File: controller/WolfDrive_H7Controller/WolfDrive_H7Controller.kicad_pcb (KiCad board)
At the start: 4 copper layers, 167.6 x 111.8 mm, 281 parts, among them CN10 CONN_02X17, CN7 CONN_02X10, CN8 CONN_02X08, CN9 CONN_02X15, CON1 SD_Card, J1 USB_OTG, J10 GND, J11 GND, J12 5V, J13 Regen, J14 Throttle, J15 PWM1, J16 PWM2, J17 PWM3, J18 ~PWM1, J19 ~PWM2, J2 QSPI_CLK, J20 ~PWM3, J21 OCV, J22 ~F_C, J23 ~F_B, J24 ~F_A, J25 Overtemp, J26 PWM1, J27 Conn_01x04_Female, J29 Conn_01x04, J3 QSPI_NCS, J30 SPI2_SCK, J31 SPI2_NSS, J32 SPI2_MOSI, J33 SPI2_MISO, J34 PS-DIS, J35 3V3, J36 GND, J37 GND, J38 AGND, J39 SP1_MISO, J4 QSPI_IO0, J40 SP1_SCK, J41 SP1_NSS, J42 SP1_MOSI, J43 DB15_Female_HighDensity_Mount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, J5 QSPI_IO1, J6 QSPI_IO2, J7 QSPI_IO3, J8 12V, J9 GND, P10 GATE_IO_A, P11 GATE_IO_A, P7 CONN_01X02, P9 GATE_IO_A, Q2 Q_NMOS_DGS, U1 LM1117-5.0, U10 74LS136, U11 FT232RL, U2 LM1117-3.3, U3 MCP101-315D, U4 LTV-356T, U5 ISO7221, U7 OPA2340, U8 LM339, U9 CD4044B

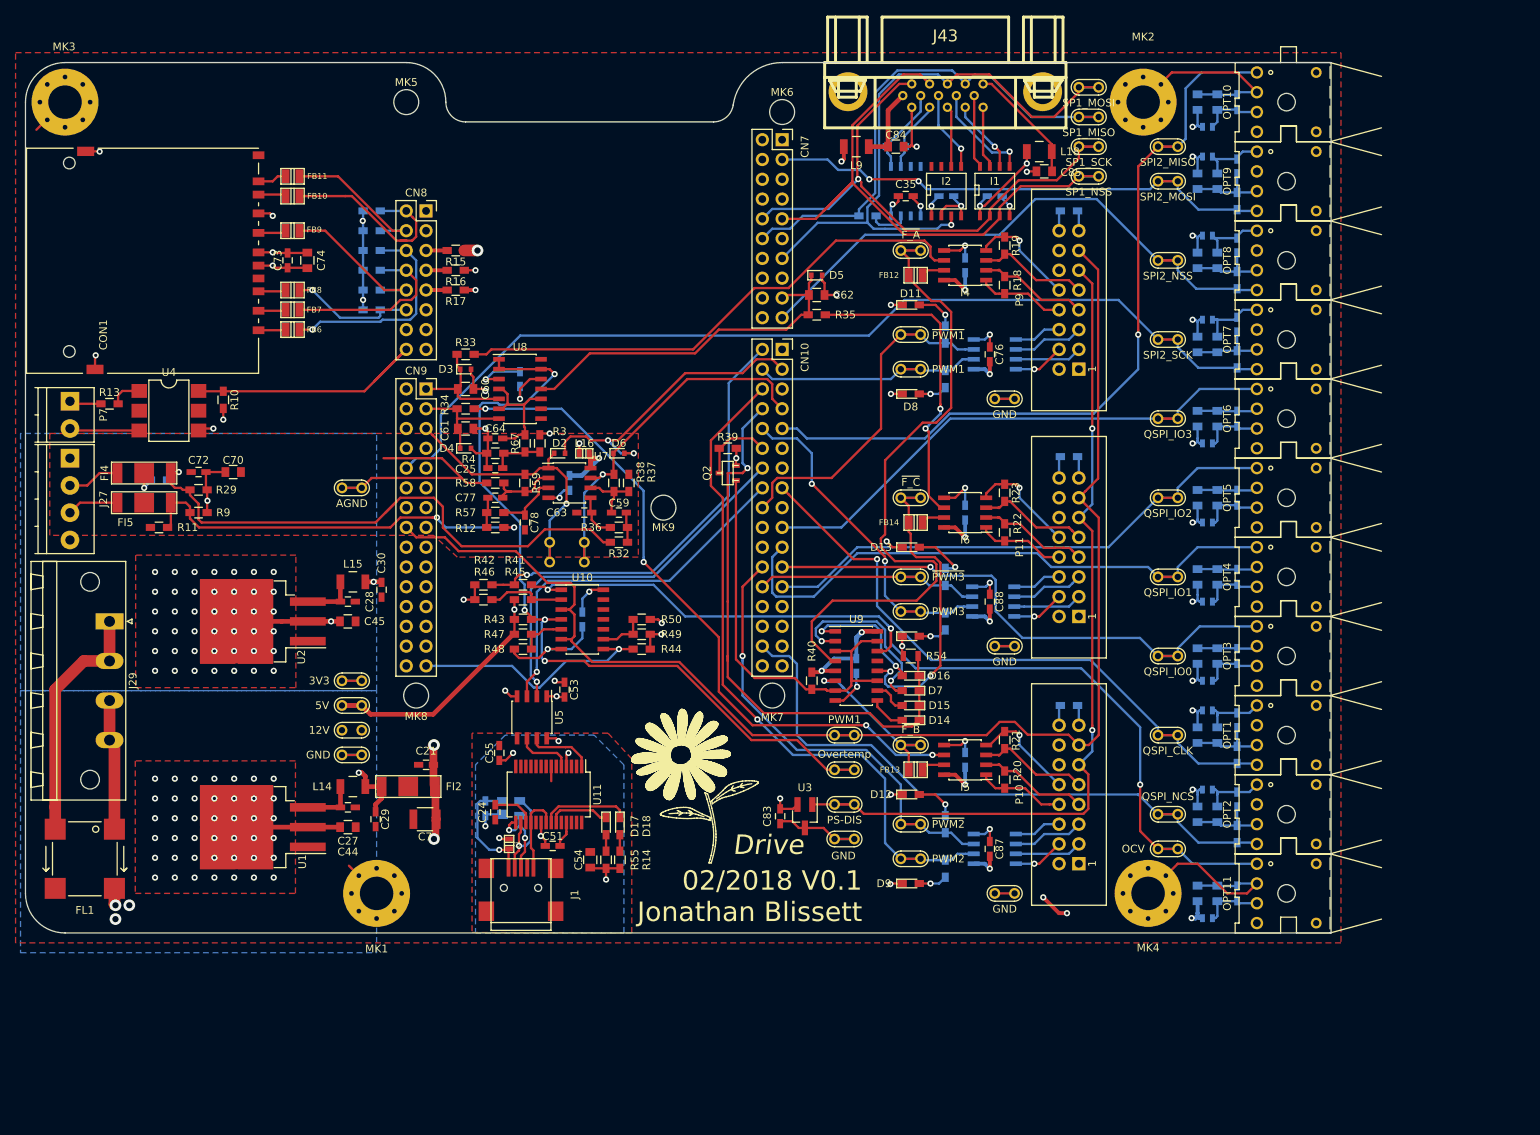
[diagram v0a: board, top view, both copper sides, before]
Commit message: PCB layout progress for issues <5
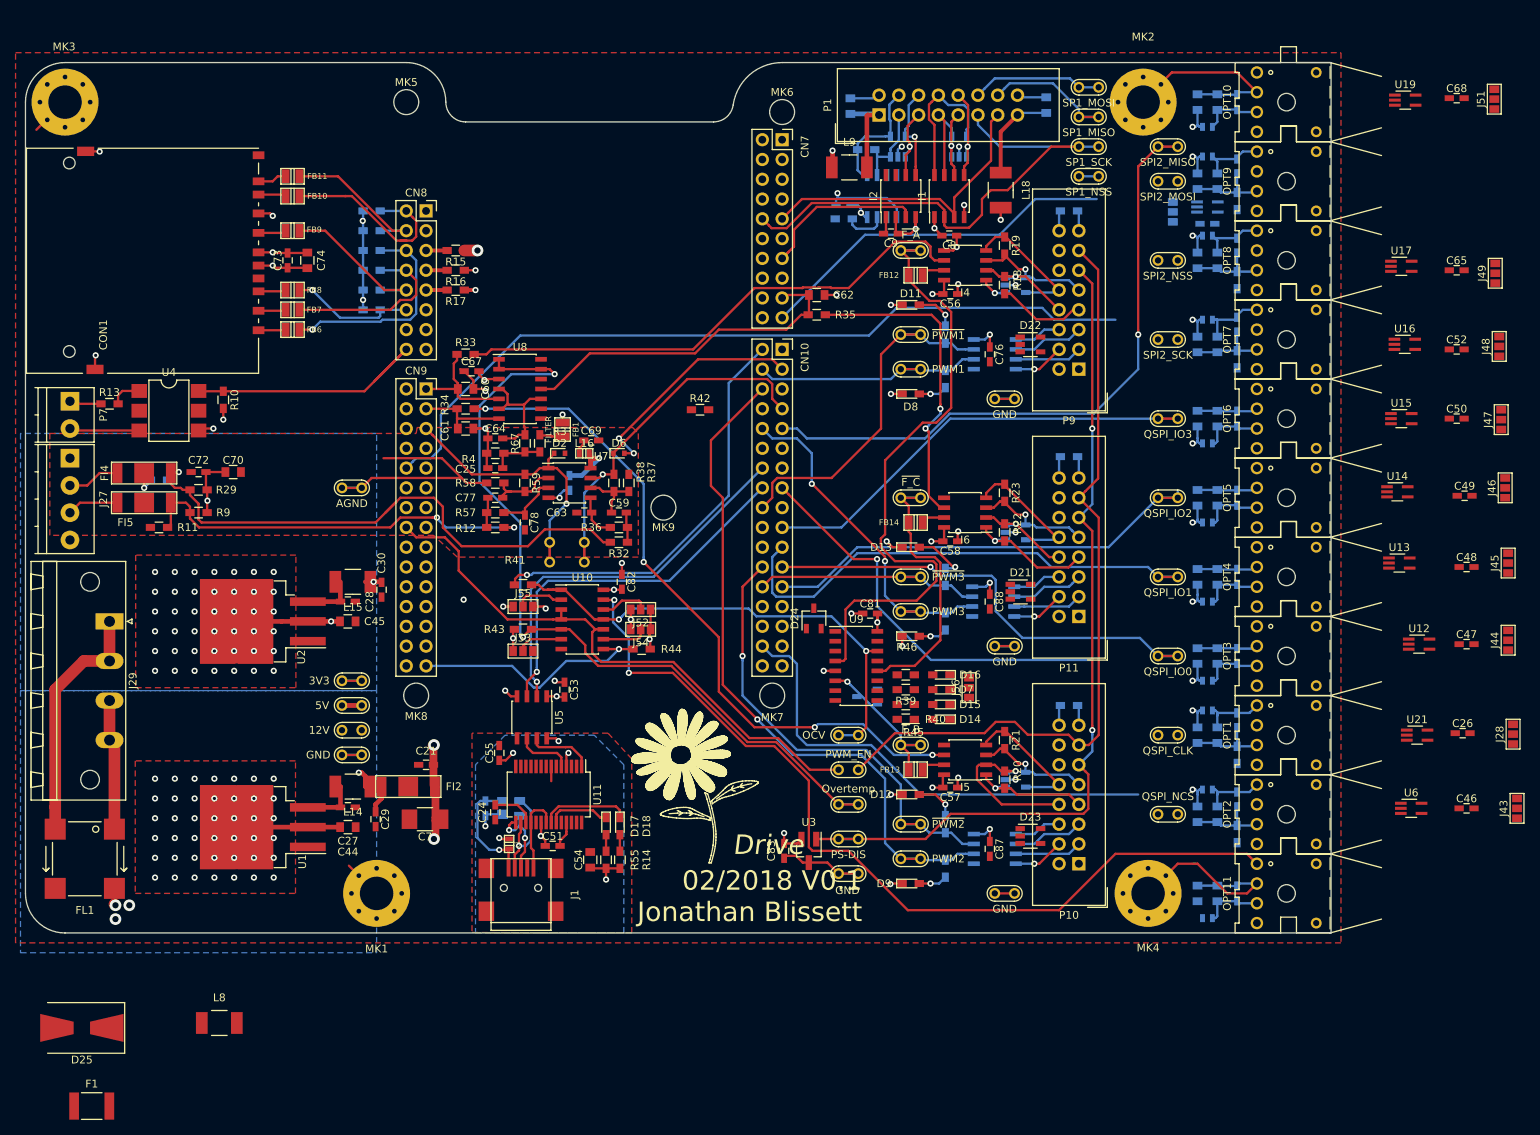
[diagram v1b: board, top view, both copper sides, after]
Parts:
- removed Q2: Q_NMOS_DGS, w_smd_trans:sot23
- removed R47, R48, R49, R50: 10k, Resistors_SMD:R_0603_HandSoldering
- removed R54: 47, Resistors_SMD:R_0805
- added C26: 10n, Capacitors_SMD:C_0603_HandSoldering, F.Cu at (134.4, 4.83)
- added C46: 10n, Capacitors_SMD:C_0603_HandSoldering, F.Cu at (134.9, 14.5)
- added C47: 10n, Capacitors_SMD:C_0603_HandSoldering, F.Cu at (134.9, -6.60)
- added C48: 10n, Capacitors_SMD:C_0603_HandSoldering, F.Cu at (134.9, -16.5)
- added C49: 10n, Capacitors_SMD:C_0603_HandSoldering, F.Cu at (134.6, -25.7)
- added C50: 10n, Capacitors_SMD:C_0603_HandSoldering, F.Cu at (133.6, -35.6)
- added C52: 10n, Capacitors_SMD:C_0603_HandSoldering, F.Cu at (133.6, -44.5)
- added C65: 10n, Capacitors_SMD:C_0603_HandSoldering, F.Cu at (133.6, -54.6)
- added C66: 10n, Capacitors_SMD:C_0603_HandSoldering, B.Cu at (101.6, -60.6)
- added C68: 10n, Capacitors_SMD:C_0603_HandSoldering, F.Cu at (133.6, -76.7)
- added C69: 1u, Capacitors_SMD:C_0603_HandSoldering, F.Cu at (22.5, -32.8)
- added D19: SP0504BAHT, TO_SOT_Packages_SMD:TSOT-23-5, B.Cu at (77.0, 10.8)
- added D20: SP0504BAHT, TO_SOT_Packages_SMD:TSOT-23-5, B.Cu at (77.0, -21.0)
- added D21: SP0504BAHT, TO_SOT_Packages_SMD:TSOT-23-5, F.Cu at (77.6, -13.3)
- added D22: SP0504BAHT, TO_SOT_Packages_SMD:TSOT-23-5, F.Cu at (78.9, -45.1)
- added D23: SP0504BAHT, TO_SOT_Packages_SMD:TSOT-23-5, F.Cu at (78.9, 18.0)
- added D24: D_Schottky_x2_KCom_AAK, TO_SOT_Packages_SMD:TSOT-23, F.Cu at (51.1, -9.91)
- added D25: 1.5KExxA, Diode_SMD:D_SMB-SMC_Universal_Handsoldering, F.Cu at (-42.9, 42.7)
- added D26: D_Schottky_x2_KCom_AAK, TO_SOT_Packages_SMD:TSOT-23, B.Cu at (57.9, 0.13)
- added F1: Polyfuse, Fuse:Fuse_1812_4532Metric_Pad1.24x3.50mm_HandSolder, F.Cu at (-41.7, 52.7)
- added FB1: FILTER, w_smd_inductors:inductor_smd_0805, F.Cu at (18.8, -34.2)
- added J28: GS3, Connectors:GS3, F.Cu at (140.8, 4.95)
- added J44: GS3, Connectors:GS3, F.Cu at (140.2, -7.11)
- added J45: GS3, Connectors:GS3, F.Cu at (140.2, -17.0)
- added J46: GS3, Connectors:GS3, F.Cu at (139.8, -26.7)
- added J47: GS3, Connectors:GS3, F.Cu at (139.3, -35.4)
- added J48: GS3, Connectors:GS3, F.Cu at (139.1, -44.8)
- added J49: GS3, Connectors:GS3, F.Cu at (138.6, -54.2)
- added J50: GS3, Connectors:GS3, B.Cu at (97.2, -62.1)
- added J51: GS3, Connectors:GS3, F.Cu at (138.4, -76.6)
- added J52: GS3, Connectors:GS3, F.Cu at (28.8, -11.0)
- added J53: GS3, Connectors:GS3, F.Cu at (13.7, -5.71)
- added J54: GS3, Connectors:GS3, F.Cu at (28.8, -8.51)
- added J55: GS3, Connectors:GS3, F.Cu at (13.7, -11.4)
- added J56: GS3, Connectors:GS3, F.Cu at (71.0, -1.02)
- added L8: 10uH, Inductors_NEOSID:Neosid_Inductor_SM-NE45_SMD1812, F.Cu at (-25.3, 42.0)
- added P1: GATE_IO_A, Connectors_IDC:IDC-Header_2x08_Pitch2.54mm_Straight, F.Cu at (59.4, -74.5)
- added U12: 74LVC1G02, TO_SOT_Packages_SMD:SOT-353_SC-70-5_Handsoldering, F.Cu at (128.8, -6.60)
- added U13: 74LVC1G02, TO_SOT_Packages_SMD:SOT-353_SC-70-5_Handsoldering, F.Cu at (126.2, -17.0)
- added U14: 74LVC1G02, TO_SOT_Packages_SMD:SOT-353_SC-70-5_Handsoldering, F.Cu at (126.0, -26.2)
- added U15: 74LVC1G02, TO_SOT_Packages_SMD:SOT-353_SC-70-5_Handsoldering, F.Cu at (126.5, -35.6)
- added U16: 74LVC1G02, TO_SOT_Packages_SMD:SOT-353_SC-70-5_Handsoldering, F.Cu at (126.9, -45.1)
- added U17: 74LVC1G02, TO_SOT_Packages_SMD:SOT-353_SC-70-5_Handsoldering, F.Cu at (126.5, -55.1)
- added U18: 74LVC1G02, TO_SOT_Packages_SMD:SOT-353_SC-70-5_Handsoldering, B.Cu at (101.6, -62.7)
- added U19: 74LVC1G02, TO_SOT_Packages_SMD:SOT-353_SC-70-5_Handsoldering, F.Cu at (127.0, -76.5)
- added U21: 74LVC1G02, TO_SOT_Packages_SMD:SOT-353_SC-70-5_Handsoldering, F.Cu at (128.5, 5.08)
- added U6: 74LVC1G02, TO_SOT_Packages_SMD:SOT-353_SC-70-5_Handsoldering, F.Cu at (127.8, 14.5)
- C27, C28: value 100n -> 1u
- C29: value 1u -> 100n
- C35, C84, C85: moved to B.Cu
- C56, C57, C58, C67, C8, C81, C82, C9: moved to F.Cu
- C7: footprint Capacitors_SMD:C_1210 -> Capacitors_SMD:C_1210_HandSoldering
- D3, D4, D5: value 3.3V -> SP0504BAHT; footprint Diodes_SMD:D_SOD-523 -> TO_SOT_Packages_SMD:TSOT-23-5; moved to B.Cu
- I1, I2, I3: footprint SMD_Packages:SOIC-8-N -> Housings_SOIC:SOIC-8_3.9x4.9mm_Pitch1.27mm
- J26: value PWM1 -> PWM_EN
- J43: value DB15_Female_HighDensity_MountingHoles -> GS3; footprint DriveParts:DB_15F-VGA-mountingholes -> Connectors:GS3
- L14, L15, L18, L9: footprint Inductors_NEOSID:Neosid_Inductor_SM-NE30_SMD1210 -> Inductors_NEOSID:Neosid_Inductor_SM-NE45_SMD1812
- P10, P11, P9: footprint Connectors:IDC_Header_Straight_16pins -> Connectors_IDC:IDC-Header_2x08_Pitch2.54mm_Straight
- R33, R34, R35: value 10k -> 4k7
- R39, R40, R45, R46: value 10k -> 680
- R60, R61, R62, R63, R64, R65: value 100 -> 680; footprint LEDs:LED_0603_HandSoldering -> Resistors_SMD:R_0603_HandSoldering
- R8: value 250 -> 240
- U10: value 74LS136 -> 74HC266
- U9: value CD4044B -> CD4043B
- moved J43 119.7 mm to (141.4, 14.5), turned to 0 degrees
- moved D3 69.5 mm to (69.7, -70.5), turned to 90 degrees
- moved D4 67.7 mm to (61.8, -70.5), turned to 90 degrees
- moved R46 55.1 mm to (62.9, -2.67)
- moved R45 51.0 mm to (62.9, 1.14), turned to 180 degrees
- moved J21 43.5 mm to (54.2, 5.08)
- moved R39 38.5 mm to (62.9, -0.76), turned to 180 degrees
- moved R42 35.8 mm to (36.4, -36.7), turned to 0 degrees
- moved D5 25.6 mm to (77.0, -52.7)
- moved R40 13.0 mm to (62.9, 3.05), turned to 180 degrees
- moved C9 8.59 mm to (61.0, -59.3)
- moved C85 8.51 mm to (80.9, -75.8), turned to 90 degrees
- moved C35 8.08 mm to (54.9, -63.0), turned to 0 degrees
- moved C84 7.83 mm to (55.8, -75.7), turned to 90 degrees
- moved C8 7.74 mm to (68.5, -59.1)
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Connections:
- net /5V_thr renamed /12V_thr
- net /~Fault_Gate_A renamed /Fault_Gate_A
- net /~Fault_Gate_B renamed /Fault_Gate_B
- net /~Fault_Gate_C renamed /Fault_Gate_C
- C56 pad 2: +5V -> +3V3
- C57 pad 2: +5V -> +3V3
- C58 pad 2: +5V -> +3V3
- C67 pad 2: +5V -> +3V3
- C76 pad 2: +5V -> +3V3
- C79 pad 2: +5V -> +3V3
- C81 pad 2: +5V -> +3V3
- C82 pad 2: +5V -> +3V3
- C87 pad 2: +5V -> +3V3
- C88 pad 2: +5V -> +3V3
- CN10 pad 1: Net-(CN10-Pad1) -> (no net)
- CN10 pad 11: Net-(CN10-Pad11) -> (no net)
- CN10 pad 13: Net-(CN10-Pad13) -> (no net)
- CN10 pad 20: Net-(CN10-Pad20) -> (no net)
- CN10 pad 28: Net-(CN10-Pad28) -> (no net)
- CN10 pad 29: Net-(CN10-Pad29) -> (no net)
- CN10 pad 30: Net-(CN10-Pad30) -> (no net)
- CN10 pad 31: Net-(CN10-Pad31) -> (no net)
- CN10 pad 33: Net-(CN10-Pad33) -> (no net)
- CN10 pad 34: Net-(CN10-Pad34) -> (no net)
- CN7 pad 1: Net-(CN7-Pad1) -> (no net)
- CN7 pad 11: Net-(CN7-Pad11) -> (no net)
- CN7 pad 14: Net-(CN7-Pad14) -> (no net)
- CN7 pad 15: Net-(CN7-Pad15) -> (no net)
- CN7 pad 16: Net-(CN7-Pad16) -> (no net)
- CN7 pad 18: Net-(CN7-Pad18) -> (no net)
- CN7 pad 2: Net-(CN7-Pad2) -> (no net)
- CN7 pad 20: Net-(CN7-Pad20) -> (no net)
- CN7 pad 4: Net-(CN7-Pad4) -> (no net)
- CN7 pad 5: Net-(CN7-Pad5) -> (no net)
- CN7 pad 6: Net-(CN7-Pad6) -> (no net)
- CN7 pad 7: Net-(CN7-Pad7) -> (no net)
- CN8 pad 1: Net-(CN8-Pad1) -> (no net)
- CN8 pad 14: Net-(CN8-Pad14) -> (no net)
- CN8 pad 15: Net-(CN8-Pad15) -> (no net)
- CN8 pad 3: Net-(CN8-Pad3) -> (no net)
- CN9 pad 11: Net-(CN9-Pad11) -> (no net)
- CN9 pad 12: Net-(CN9-Pad12) -> (no net)
- CN9 pad 13: Net-(CN9-Pad13) -> (no net)
- CN9 pad 14: Net-(CN9-Pad14) -> (no net)
- CN9 pad 15: Net-(CN9-Pad15) -> (no net)
- CN9 pad 17: Net-(CN9-Pad17) -> (no net)
- CN9 pad 18: Net-(CN9-Pad18) -> (no net)
- CN9 pad 19: Net-(CN9-Pad19) -> (no net)
- CN9 pad 2: Net-(CN9-Pad2) -> (no net)
- CN9 pad 20: Net-(CN9-Pad20) -> (no net)
- CN9 pad 21: Net-(CN9-Pad21) -> (no net)
- CN9 pad 22: Net-(CN9-Pad22) -> (no net)
- CN9 pad 24: Net-(CN9-Pad24) -> (no net)
- CN9 pad 25: Net-(CN9-Pad25) -> (no net)
- CN9 pad 26: Net-(CN9-Pad26) -> (no net)
- CN9 pad 27: Net-(CN9-Pad27) -> (no net)
- CN9 pad 28: Net-(CN9-Pad28) -> (no net)
- CN9 pad 30: Net-(CN9-Pad30) -> (no net)
- CN9 pad 4: Net-(CN9-Pad4) -> (no net)
- CN9 pad 6: Net-(CN9-Pad6) -> (no net)
- CN9 pad 7: Net-(CN9-Pad7) -> (no net)
- CN9 pad 8: Net-(CN9-Pad8) -> (no net)
- CON1 pad 10: Net-(CON1-Pad10) -> (no net)
- CON1 pad 11: Net-(CON1-Pad11) -> (no net)
- D14 pad 1: /GPIO_EXTI14_PF14 -> Net-(D14-Pad1)
- D15 pad 1: /GPIO_EXTI14_PF14 -> Net-(D14-Pad1)
- D16 pad 1: /GPIO_EXTI14_PF14 -> Net-(D14-Pad1)
- D3 pad 1: /ADC1_INP15_PA3 -> /SPI1_NSS-
- D4 pad 1: /ADC1_INP10_PC0 -> /SP1_MOSI+
- D5 pad 1: /ADC1_INP18_PA4 -> /Fault_A+
- D7 pad 1: /GPIO_EXTI14_PF14 -> Net-(D14-Pad1)
- FL1 pad 2: +12V -> Net-(D25-Pad1)
- I2 pad 7: Net-(I2-Pad7) -> (no net)
- I2 pad 8: Net-(I2-Pad8) -> (no net)
- I3 pad 3: Net-(I3-Pad3) -> (no net)
- I3 pad 4: Net-(I3-Pad4) -> (no net)
- I3 pad 6: Net-(I3-Pad6) -> (no net)
- I4 pad 1: /~Fault_A- -> /Fault_A+
- I4 pad 2: /~Fault_A+ -> /Fault_A-
- I4 pad 8: +5V -> +3V3
- I5 pad 1: /~Fault_B- -> /Fault_B+
- I5 pad 2: /~Fault_B+ -> /Fault_B-
- I5 pad 8: +5V -> +3V3
- I6 pad 1: /~Fault_C- -> /Fault_C+
- I6 pad 2: /~Fault_C+ -> /Fault_C-
- I6 pad 8: +5V -> +3V3
- I7 pad 1: +5V -> +3V3
- I8 pad 1: +5V -> +3V3
- I9 pad 1: +5V -> +3V3
- J1 pad 4: Net-(J1-Pad4) -> (no net)
- J2 pad 1: /QUADSPI_CLK_PB2 -> Net-(J2-Pad1)
- J21 pad 1: /~Fault_OCV -> /Fault_OCV
- J3 pad 1: /QUADSPI_BK1_NCS_PB10 -> Net-(J3-Pad1)
- J30 pad 1: /SPI2_SCK_PD3 -> Net-(J30-Pad1)
- J31 pad 1: /SPI2_NSS_PB4 -> Net-(J31-Pad1)
- J32 pad 1: /SP2_MOSI_PB15 -> Net-(J32-Pad1)
- J43 pad 2: /SP1_MISO+ -> Net-(J43-Pad2)
- J43 pad 3: /SP1_MOSI+ -> +3V3
- L16 pad 2: +5V -> +12VA
- L17 pad 1: +5V -> +3V3
- OPT1 pad 2: Net-(OPT1-Pad2) -> (no net)
- OPT1 pad 4: /QUADSPI_CLK_PB2 -> Net-(J2-Pad1)
- OPT10 pad 1: /SP2_MISO_PC2 -> Net-(OPT10-Pad1)
- OPT10 pad 4: Net-(OPT10-Pad4) -> (no net)
- OPT11 pad 1: /~Fault_OCV -> Net-(OPT11-Pad1)
- OPT11 pad 4: Net-(OPT11-Pad4) -> (no net)
- OPT2 pad 2: Net-(OPT2-Pad2) -> (no net)
- OPT2 pad 4: /QUADSPI_BK1_NCS_PB10 -> Net-(J3-Pad1)
- OPT3 pad 1: /QUADSPI_BK1_IO0_PD11 -> Net-(OPT3-Pad1)
- OPT3 pad 4: Net-(OPT3-Pad4) -> (no net)
- OPT4 pad 1: /QUADSPI_BK1_IO1_PD12 -> Net-(OPT4-Pad1)
- OPT4 pad 4: Net-(OPT4-Pad4) -> (no net)
- OPT5 pad 1: /QUADSPI_BK1_IO2_PE2 -> Net-(OPT5-Pad1)
- OPT5 pad 4: Net-(OPT5-Pad4) -> (no net)
- OPT6 pad 1: /QUADSPI_BK1_IO3_PD13 -> Net-(OPT6-Pad1)
- OPT6 pad 4: Net-(OPT6-Pad4) -> (no net)
- OPT7 pad 2: Net-(OPT7-Pad2) -> (no net)
- OPT7 pad 4: /SPI2_SCK_PD3 -> Net-(J30-Pad1)
- OPT8 pad 2: Net-(OPT8-Pad2) -> (no net)
- OPT8 pad 4: /SPI2_NSS_PB4 -> Net-(J31-Pad1)
- OPT9 pad 2: Net-(OPT9-Pad2) -> (no net)
- OPT9 pad 4: /SP2_MOSI_PB15 -> Net-(J32-Pad1)
- P10 pad 7: /~Fault_B+ -> /Fault_B+
- P10 pad 8: /~Fault_B- -> /Fault_B-
- P11 pad 7: /~Fault_C+ -> /Fault_C+
- P11 pad 8: /~Fault_C- -> /Fault_C-
- P9 pad 7: /~Fault_A+ -> /Fault_A+
- P9 pad 8: /~Fault_A- -> /Fault_A-
- R1 pad 2: /QUADSPI_CLK_PB2 -> Net-(J2-Pad1)
- R18 pad 1: /~Fault_A+ -> /Fault_A-
- R18 pad 2: /~Fault_A- -> /Fault_A+
- R2 pad 2: /QUADSPI_BK1_NCS_PB10 -> Net-(J3-Pad1)
- R20 pad 1: /~Fault_B+ -> /Fault_B-
- R20 pad 2: /~Fault_B- -> /Fault_B+
- R22 pad 1: /~Fault_C+ -> /Fault_C-
- R22 pad 2: /~Fault_C- -> /Fault_C+
- R3 pad 2: +5V -> Net-(FB1-Pad2)
- R39 pad 1: /GPIO_OUTPUT_PF15 -> Net-(D7-Pad2)
- R39 pad 2: DGND -> Net-(D24-Pad1)
- R40 pad 1: +5V -> Net-(D14-Pad2)
- R40 pad 2: Net-(Q2-Pad1) -> Net-(D26-Pad2)
- R41 pad 1: /~Fault_OCV -> /Fault_OCV
- R42 pad 1: /GPIO_EXTI13_PF13 -> DGND
- R42 pad 2: DGND -> /GPIO_EXTI14_PF14
- R43 pad 1: +5V -> +3V3
- R44 pad 1: +5V -> +3V3
- R45 pad 1: +5V -> Net-(D15-Pad2)
- R45 pad 2: Net-(R45-Pad2) -> Net-(D26-Pad1)
- R46 pad 1: Net-(R45-Pad2) -> Net-(D16-Pad2)
- R46 pad 2: DGND -> Net-(D24-Pad2)
- R5 pad 2: /SPI2_SCK_PD3 -> Net-(J30-Pad1)
- R6 pad 2: /SPI2_NSS_PB4 -> Net-(J31-Pad1)
- R7 pad 2: /SP2_MOSI_PB15 -> Net-(J32-Pad1)
- U10 pad 1: /~Fault_OCV -> /Fault_OCV
- U10 pad 10: (no net) -> /PWM_EN
- U10 pad 11: (no net) -> /Fault_OCV
- U10 pad 12: (no net) -> Net-(J52-Pad2)
- U10 pad 13: (no net) -> Net-(OPT11-Pad1)
- U10 pad 14: +5V -> +3V3
- U10 pad 2: Net-(R45-Pad2) -> Net-(J55-Pad2)
- U10 pad 4: /OverTemp_trip -> /PWM_EN
- U10 pad 5: Net-(R47-Pad2) -> /OverTemp_trip
- U10 pad 6: /PWM_EN -> Net-(J53-Pad2)
- U11 pad 10: Net-(U11-Pad10) -> (no net)
- U11 pad 11: Net-(U11-Pad11) -> (no net)
- U11 pad 12: Net-(U11-Pad12) -> (no net)
- U11 pad 13: Net-(U11-Pad13) -> (no net)
- U11 pad 14: Net-(U11-Pad14) -> (no net)
- U11 pad 19: Net-(U11-Pad19) -> (no net)
- U11 pad 2: Net-(U11-Pad2) -> (no net)
- U11 pad 26: Net-(U11-Pad26) -> Net-(C10-Pad2)
- U11 pad 27: Net-(U11-Pad27) -> (no net)
- U11 pad 28: Net-(U11-Pad28) -> (no net)
- U11 pad 3: Net-(U11-Pad3) -> (no net)
- U11 pad 6: Net-(U11-Pad6) -> (no net)
- U11 pad 9: Net-(U11-Pad9) -> (no net)
- U8 pad 3: +5V -> +3V3
- U9 pad 1: Net-(D16-Pad2) -> Net-(D24-Pad2)
- U9 pad 10: Net-(D15-Pad2) -> Net-(D26-Pad1)
- U9 pad 11: Net-(Q2-Pad1) -> /GPIO_OUTPUT_PF15
- U9 pad 14: /~Fault_OCV -> /Fault_OCV
- U9 pad 15: Net-(Q2-Pad1) -> /GPIO_OUTPUT_PF15
- U9 pad 16: +5V -> +3V3
- U9 pad 2: Net-(D7-Pad2) -> Net-(D24-Pad1)
- U9 pad 3: Net-(Q2-Pad1) -> /GPIO_OUTPUT_PF15
- U9 pad 5: +5V -> +3V3
- U9 pad 7: Net-(Q2-Pad1) -> /GPIO_OUTPUT_PF15
- U9 pad 9: Net-(D14-Pad2) -> Net-(D26-Pad2)
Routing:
- net +5V: track 445.5 -> 97.2 mm, vias 61 -> 44
- net /~Fault_OCV: track 130.6 -> 0.38 mm, vias 3 -> 0
- net Net-(OPT11-Pad1): track 0.00 -> 113.5 mm, vias 0 -> 2
- net /GPIO_EXTI14_PF14: track 74.4 -> 0.00 mm, vias 1 -> 0
- net /SP2_MOSI_PB15: track 72.7 -> 0.00 mm, vias 2 -> 0
- net /Fault_OCV: track 0.00 -> 69.7 mm, vias 0 -> 2
- net Net-(Q2-Pad1): track 56.3 -> 0.00 mm
- net /SP1_MISO_PA6: track 71.3 -> 23.6 mm
- net /SP1_MOSI_PB5: track 84.5 -> 44.9 mm, vias 1 -> 0
- net /QUADSPI_CLK_PB2: track 88.0 -> 52.3 mm
- net /SPI1_NSS_PA15: track 82.7 -> 47.4 mm
- net /SPI2_NSS_PB4: track 80.5 -> 46.7 mm
- net /SPI2_SCK_PD3: track 132.6 -> 102.7 mm
- net /QUADSPI_BK1_NCS_PB10: track 87.6 -> 61.5 mm
- net DGND: track 323.6 -> 299.4 mm, vias 33 -> 36
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
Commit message: Major PCB layout revision for v0.2
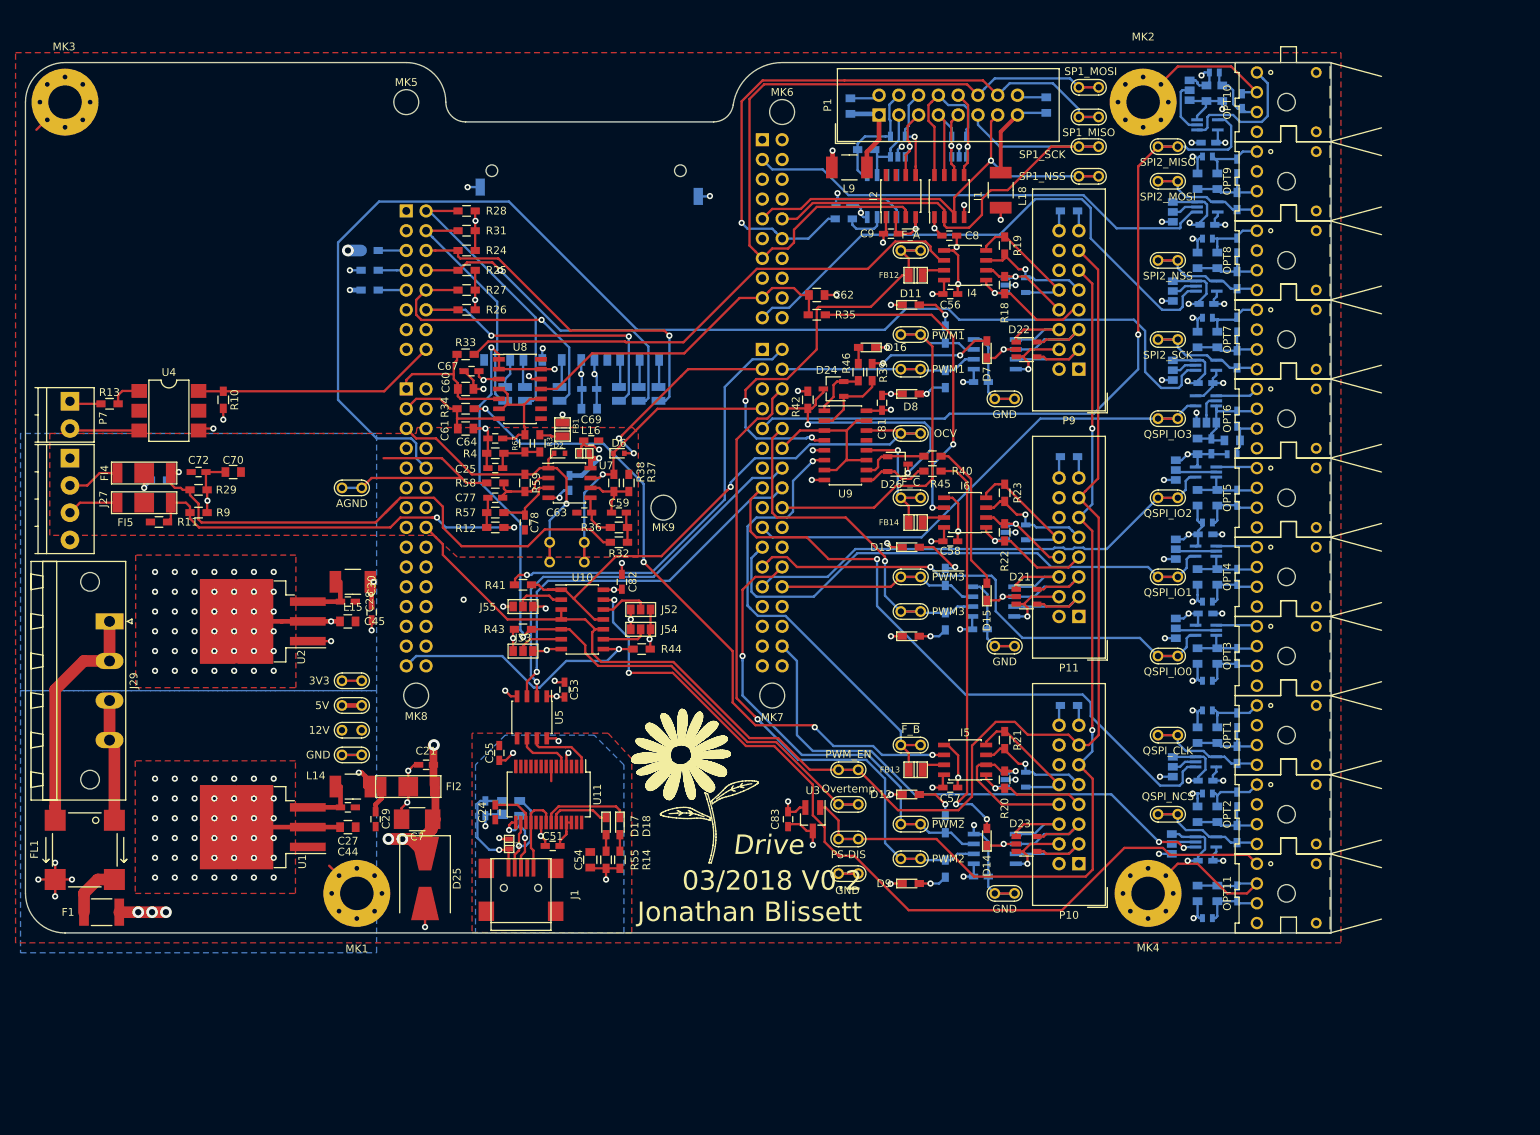
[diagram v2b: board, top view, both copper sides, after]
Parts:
- removed C50: 10n, Capacitors_SMD:C_0603_HandSoldering
- removed J56: GS3, Connectors:GS3
- removed L8: 10uH, Inductors_NEOSID:Neosid_Inductor_SM-NE45_SMD1812
- C26, C46, C47, C48, C49, C52, C65, C68, C73, C74, C76, C87, C88, CN10, CN7, CN8, CN9, CON1, FB10, FB11, FB6, FB7, FB8, FB9, J28, J43, J44, J45, J46, J47, J48, J49, J51, R15, R16, R17, U12, U13, U14, U15, U16, U17, U19, U21, U6: moved to B.Cu
- D26, R24, R25, R26, R27, R28, R31: moved to F.Cu
- moved CON1 54.6 mm to (22.2, -55.2), turned to 0 degrees
- moved D25 48.1 mm to (1.14, 23.5), turned to 270 degrees
- moved FB6 47.7 mm to (31.1, -38.7), turned to 90 degrees
- moved FB7 45.7 mm to (28.6, -38.7), turned to 90 degrees
- moved J43 44.6 mm to (97.0, 19.1), turned to 180 degrees
- moved D7 44.1 mm to (73.3, -44.4), turned to 90 degrees
- moved FB8 44.0 mm to (26.0, -38.7), turned to 90 degrees
- moved J28 43.9 mm to (97.2, 9.14), turned to 180 degrees
- moved D16 43.1 mm to (57.9, -44.7)
- moved J45 42.7 mm to (97.5, -18.8), turned to 180 degrees
- moved J44 42.7 mm to (97.5, -8.64), turned to 180 degrees
- moved J46 42.4 mm to (97.5, -29.0), turned to 180 degrees
- moved C73 42.1 mm to (22.2, -39.4), turned to 180 degrees
- moved J48 42.0 mm to (97.2, -41.8), turned to 180 degrees
- moved J49 41.5 mm to (97.2, -51.9), turned to 180 degrees
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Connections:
- C29 pad 1: Net-(C29-Pad1) -> +12VA
- C30 pad 1: Net-(C29-Pad1) -> +12VA
- D14 pad 1: Net-(D14-Pad1) -> DGND
- D15 pad 1: Net-(D14-Pad1) -> DGND
- D16 pad 1: Net-(D14-Pad1) -> DGND
- D21 pad 1: /PWMC_HS- -> /PWMC_LS-
- D21 pad 3: /PWMC_HS+ -> /PWMC_HS-
- D21 pad 5: /PWMC_LS- -> /PWMC_LS+
- D22 pad 1: /PWMA_HS- -> /PWMA_LS-
- D22 pad 3: /PWMA_HS+ -> /PWMA_HS-
- D22 pad 5: /PWMA_LS- -> /PWMA_LS+
- D23 pad 1: /PWMB_HS- -> /PWMB_LS-
- D23 pad 3: /PWMB_HS+ -> /PWMB_HS-
- D23 pad 5: /PWMB_LS- -> /PWMB_LS+
- D25 pad 1: Net-(D25-Pad1) -> +12V
- D7 pad 1: Net-(D14-Pad1) -> DGND
- F1 pad 2: Net-(D25-Pad1) -> Net-(F1-Pad2)
- FI2 pad 3: Net-(C29-Pad1) -> +12VA
- FL1 pad 2: Net-(D25-Pad1) -> Net-(F1-Pad2)
- L14 pad 1: Net-(C29-Pad1) -> +12VA
- L15 pad 1: Net-(C29-Pad1) -> +12VA
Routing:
- net DGND: track 299.4 -> 437.6 mm, vias 36 -> 63
- net +5V: track 97.2 -> 203.4 mm
- net +12VA: track 1.89 -> 84.1 mm, vias 0 -> 3
- net /SP1_MISO_PA6: track 23.6 -> 87.9 mm, vias 0 -> 1
- net /SPI2_SCK_PD3: track 102.7 -> 165.4 mm
- net /SP2_MOSI_PB15: track 0.00 -> 60.7 mm
- net /SP1_MOSI_PB5: track 44.9 -> 100.3 mm
- net +3V3: track 126.0 -> 180.1 mm, vias 74 -> 92
- net Net-(D14-Pad2): track 0.00 -> 51.8 mm, vias 0 -> 2
- net Net-(C29-Pad1): track 40.3 -> 0.00 mm, vias 2 -> 0
- net /Fault_Gate_B: track 26.3 -> 65.8 mm
- net /GPIO_EXTI14_PF14: track 0.00 -> 33.3 mm, vias 0 -> 2
- net /QUADSPI_CLK_PB2: track 52.3 -> 83.3 mm
- net /Fault_Gate_A: track 87.6 -> 59.6 mm, vias 0 -> 2
- net /SPI2_NSS_PB4: track 46.7 -> 72.0 mm
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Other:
- board text added: "03/2018 V0.2 Jonathan Blissett"
- board text added: "Isolate?"
